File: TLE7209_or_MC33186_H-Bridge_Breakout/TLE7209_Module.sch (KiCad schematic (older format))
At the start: 12 parts, among them J1 Conn_02x06_Odd_Even, J3 Conn_01x01, U1 TLE7209-2R

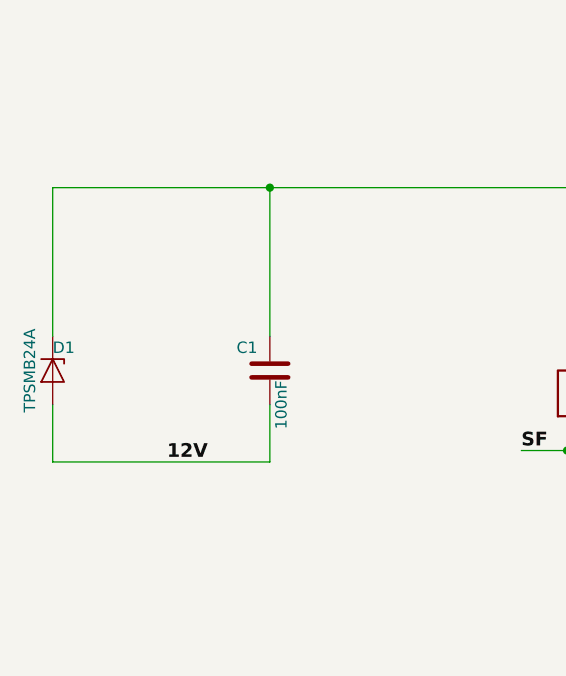
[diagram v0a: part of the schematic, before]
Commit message: Corrected schematic with LSLC Parts numbers (#25)
* Small update

* Updated with LSLC Pn

* pdf

* Pcb Update

* Gerbers

* larger cap
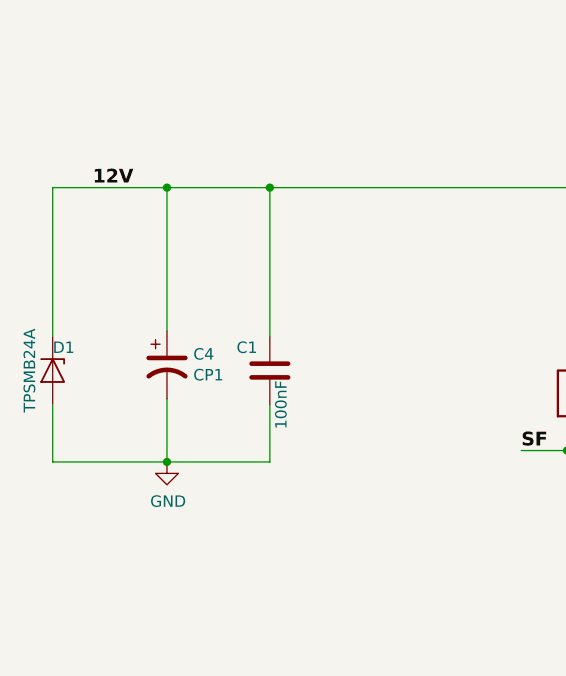
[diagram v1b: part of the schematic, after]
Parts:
- added C4: CP1, Capacitor_SMD:CP_Elec_8x6.7, symbol Device:CP1
- C1: LSLC (none) -> C49678; Part # 885012008026 -> (none); VEND MOUSER -> (none); VEND# 710-885012008026 -> (none)
- C2: LSLC (none) -> C1739; Part # 885012008026 -> (none); VEND MOUSER -> (none); VEND# 710-885012008026 -> (none)
- C3: LSLC (none) -> C1710; Part # 885012208052 -> (none); VEND MOUSER -> (none); VEND# 710-885012208052 -> (none)
- D1: Part # TPSMB24A -> (none); Part Manufacturer Littelfuse -> (none); VEND MOUSER -> (none)
- R1: LSLC (none) -> C17713
- R2: LSLC (none) -> C17514
- R3: LSLC (none) -> C17673
- R4, R5: LSLC (none) -> C17414
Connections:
- net 12V: now also C1.1, C2.1, D1.1 (K), R2.1, U1.16 (Vss), U1.5 (Vss), C4.1; no longer C1.2, D1.2 (A)
- net GND: now also C1.2, D1.2 (A), C4.2
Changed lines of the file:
@@
 F 2 "Capacitor_SMD:C_0805_2012Metric_Pad1.15x1.40mm_HandSolder" H 7300 2050 50  0001 C CNN
 F 3 "~" H 7300 2050 50  0001 C CNN
-F 4 "885012008026" H 2350 -850 50  0001 C CNN "Part #"
-F 5 "MOUSER" H 2350 -850 50  0001 C CNN "VEND"
-F 6 "710-885012008026" H 2350 -850 50  0001 C CNN "VEND#"
+F 4 " C1739" H 0   0   50  0001 C CNN "LSLC"
 	1    7300 2050
 	1    0    0    -1
@@
 F 2 "Resistor_SMD:R_0805_2012Metric_Pad1.15x1.40mm_HandSolder" H 7550 2050 50  0001 C CNN
 F 3 "~" H 7550 2050 50  0001 C CNN
+F 4 " C17514" H 0   0   50  0001 C CNN "LSLC"
 	1    7550 2050
 	1    0    0    -1
@@
 F 2 "Resistor_SMD:R_0805_2012Metric_Pad1.15x1.40mm_HandSolder" H 8200 3550 50  0001 C CNN
 F 3 "~" H 8200 3550 50  0001 C CNN
+F 4 " C17673" H 0   0   50  0001 C CNN "LSLC"
 	1    8200 3550
 	1    0    0    -1
@@
 F 2 "Capacitor_SMD:C_0805_2012Metric_Pad1.15x1.40mm_HandSolder" H 8500 3550 50  0001 C CNN
 F 3 "~" H 8500 3550 50  0001 C CNN
-F 4 "885012208052" H 2900 0   50  0001 C CNN "Part #"
-F 5 "MOUSER" H 2900 0   50  0001 C CNN "VEND"
-F 6 "710-885012208052" H 2900 0   50  0001 C CNN "VEND#"
+F 4 " C1710" H 0   0   50  0001 C CNN "LSLC"
 	1    8500 3550
 	1    0    0    -1
@@
 F 2 "Resistor_SMD:R_0805_2012Metric_Pad1.15x1.40mm_HandSolder" V 4680 2800 30  0001 C CNN
 F 3 "" H 4750 2800 30  0000 C CNN
+F 4 " C17713" H 0   0   50  0001 C CNN "LSLC"
 	1    4750 2800
 	1    0    0    -1
@@
 F 2 "Capacitor_SMD:C_0805_2012Metric_Pad1.15x1.40mm_HandSolder" H 3450 2700 50  0001 C CNN
 F 3 "~" H 3450 2700 50  0001 C CNN
-F 4 "885012008026" H -1500 -200 50  0001 C CNN "Part #"
-F 5 "MOUSER" H -1500 -200 50  0001 C CNN "VEND"
-F 6 "710-885012008026" H -1500 -200 50  0001 C CNN "VEND#"
+F 4 "C49678" H 0   0   50  0001 C CNN "LSLC"
 	1    3450 2700
 	1    0    0    -1
@@
 F 2 "Diode_SMD:D_SMA" H 2500 2500 50  0001 C CNN
 F 3 "https://www.vishay.com/docs/88301/15ke.pdf" H 2450 2700 50  0001 C CNN
-F 4 "TPSMB24A" H 50  -2450 50  0001 C CNN "Part #"
-F 5 "Littelfuse" H 50  -2450 50  0001 C CNN "Part Manufacturer"
-F 6 "MOUSER" H 50  -2450 50  0001 C CNN "VEND"
-F 7 "576-TPSMB24A" H 50  -2450 50  0001 C CNN "VEND#"
+F 4 "576-TPSMB24A" H 50  -2450 50  0001 C CNN "VEND#"
 	1    2500 2700
 	0    1    1    0
@@
 	4750 2650 4750 2550
 Wire Wire Line
-	2500 3100 3450 3100
-Wire Wire Line
-	2500 1900 3450 1900
+	2500 3100 3000 3100
+Wire Wire Line
+	2500 1900 3000 1900
 Text Label 8700 3300 0    60   ~ 12
 OUT1
@@
 Text Label 8700 1500 2    60   ~ 12
 OUT2
-Text Label 3000 3100 0    60   ~ 12
+Text Label 2675 1900 0    60   ~ 12
 12V
 Text Label 9200 1900 0    60   ~ 12
@@
 F 2 "Resistor_SMD:R_0805_2012Metric_Pad1.15x1.40mm_HandSolder" H 5250 3750 50  0001 C CNN
 F 3 "~" H 5250 3750 50  0001 C CNN
+F 4 " C17414" H 0   0   50  0001 C CNN "LSLC"
 	1    5250 3750
 	0    1    1    0
@@
 F 2 "Resistor_SMD:R_0805_2012Metric_Pad1.15x1.40mm_HandSolder" H 5800 4100 50  0001 C CNN
 F 3 "~" H 5800 4100 50  0001 C CNN
+F 4 " C17414" H 0   0   50  0001 C CNN "LSLC"
 	1    5800 4100
 	-1   0    0    1
@@
 Wire Wire Line
 	7250 2500 7400 2500
+$Comp
+L power:GND #PWR0109
+U 1 1 5E1959D7
+P 3000 3100
+F 0 "#PWR0109" H 3000 2850 50  0001 C CNN
+F 1 "GND" H 3005 2927 50  0000 C CNN
+F 2 "" H 3000 3100 50  0001 C CNN
+F 3 "" H 3000 3100 50  0001 C CNN
+	1    3000 3100
+	1    0    0    -1
+$EndComp
+$Comp
+L Device:CP1 C4
+U 1 1 5E196218
+P 3000 2675
+F 0 "C4" H 3115 2721 50  0000 L CNN
+F 1 "CP1" H 3115 2630 50  0000 L CNN
+F 2 "Capacitor_SMD:CP_Elec_8x6.7" H 3000 2675 50  0001 C CNN
+F 3 "~" H 3000 2675 50  0001 C CNN
+	1    3000 2675
+	1    0    0    -1
+$EndComp
+Wire Wire Line
+	3000 2825 3000 3100
+Connection ~ 3000 3100
+Wire Wire Line
+	3000 3100 3450 3100
+Wire Wire Line
+	3000 2525 3000 1900
+Connection ~ 3000 1900
+Wire Wire Line
+	3000 1900 3450 1900
 $EndSCHEMATC
